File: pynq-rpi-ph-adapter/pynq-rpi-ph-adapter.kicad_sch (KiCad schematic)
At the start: 9 parts, among them J1 Conn_02x08_Odd_Even, J2 Conn_02x08_Odd_Even, J3 Conn_02x08_Odd_Even, J4 Conn_02x08_Odd_Even, J5 Conn_02x08_Odd_Even, J6 Conn_02x08_Odd_Even, J7 Conn_02x20_Odd_Even

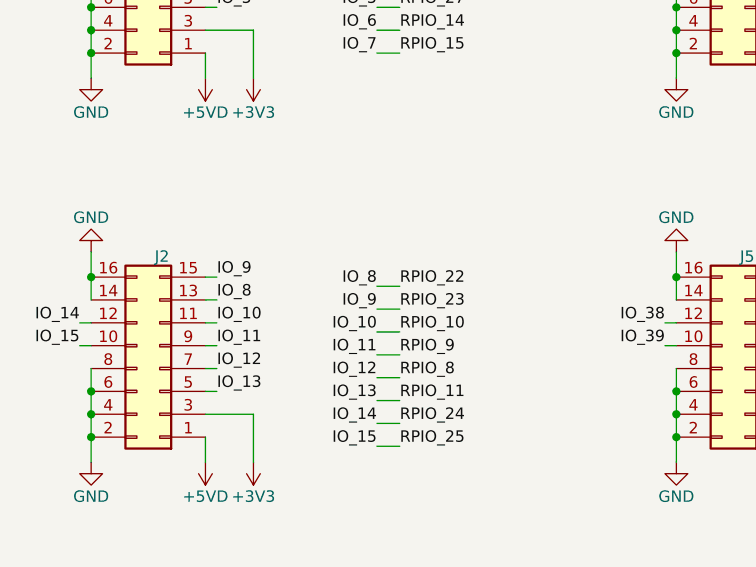
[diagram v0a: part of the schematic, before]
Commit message: Adapted and generated gerber files for pynq rpi adapter for jlcpcb
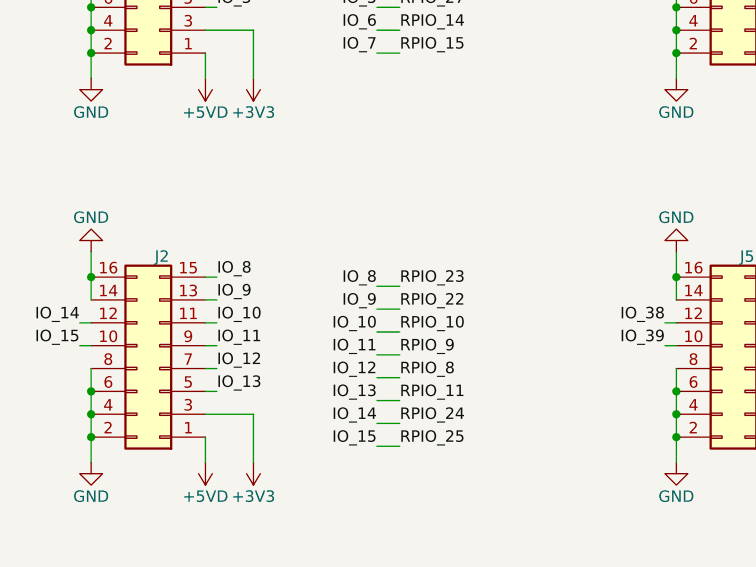
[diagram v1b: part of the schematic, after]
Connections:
- net IO_8: now also J2.15 (Pin_15), J7.16 (Pin_16); no longer J2.13 (Pin_13), J7.15 (Pin_15)
- net IO_9: now also J2.13 (Pin_13), J7.15 (Pin_15); no longer J2.15 (Pin_15), J7.16 (Pin_16)
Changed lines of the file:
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@@
     (effects (font (size 1.27 1.27)) (justify left bottom))
   )
-  (label "IO_8" (at 33.02 73.66 0)
+  (label "IO_8" (at 33.02 71.12 0)
     (effects (font (size 1.27 1.27)) (justify left bottom))
   )
@@
     (effects (font (size 1.27 1.27)) (justify right bottom))
   )
-  (label "RPIO_22" (at 53.34 72.136 0)
+  (label "RPIO_22" (at 53.34 74.676 0)
     (effects (font (size 1.27 1.27)) (justify left bottom))
   )
@@
     (effects (font (size 1.27 1.27)) (justify left bottom))
   )
-  (label "IO_9" (at 33.02 71.12 0)
+  (label "IO_9" (at 33.02 73.66 0)
     (effects (font (size 1.27 1.27)) (justify left bottom))
   )
@@
     (effects (font (size 1.27 1.27)) (justify right bottom))
   )
-  (label "RPIO_23" (at 53.34 74.676 0)
-    (effects (font (size 1.27 1.27)) (justify left bottom))
-  )
+  (label "RPIO_23" (at 53.34 72.136 0)
+    (effects (font (size 1.27 1.27)) (justify left bottom))
+  )
